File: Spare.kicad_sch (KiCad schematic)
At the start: 9 parts, among them U14 74LS125, U2 74LS14, U26 74LS06, U34 74LS393, U39 74LS04, U49 74LS07N, U5 74LS02, U59 74LS32, U8 74LS08

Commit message: rev 1.0
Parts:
- removed U34: 74LS393, Custom:STD_DDW_DIP14, symbol 74xx:74LS393
- removed U49: 74LS07N, Custom:STD_DDW_DIP14, symbol 74xx:74LS07
- removed U59: 74LS32, Custom:STD_DDW_DIP14, symbol 74xx:74LS32
- added unit 2 of U8
- added unit 1 of U8
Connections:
- no-connect marks 44 -> 34
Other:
- moved on the sheet: U39E

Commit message: V1
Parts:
- removed U39: 74LS04, Custom:STD_DDW_DIP14, symbol 74xx:74LS04
- removed unit 2 of U5
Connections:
- no-connect marks 34 -> 29
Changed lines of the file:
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@@
-	)
-	(no_connect
-		(at 231.14 124.46)
-	)
-	(no_connect
-		(at 299.72 101.6)
 	)
 	(no_connect
@@
 	)
 	(no_connect
-		(at 231.14 129.54)
-	)
-	(no_connect
 		(at 246.38 93.98)
 	)
@@
 	)
 	(no_connect
-		(at 246.38 127)
-	)
-	(no_connect
 		(at 246.38 83.82)
 	)
@@
 	)
 	(no_connect
-		(at 314.96 101.6)
-	)
-	(no_connect
 		(at 278.13 105.41)
 	)
@@
 	(no_connect
 		(at 318.77 101.6)
-	)
-	(symbol
-		(lib_id "74xx:74LS04")
-		(at 307.34 101.6 0)
-		(unit 5)
-		(exclude_from_sim no)
-		(in_bom yes)
-		(on_board yes)
-		(dnp no)
-		(property "Reference" "U39"
-			(at 307.086 99.822 0)
-			(effects
-				(font
-					(size 1.524 1.524)
-				)
-			)
-		)
-		(property "Value" "74LS04"
-			(at 307.594 103.632 0)
-			(effects
-				(font
-					(size 1.524 1.524)
-				)
-			)
-		)
-		(property "Footprint" "Custom:STD_DDW_DIP14"
-			(at 307.34 101.6 0)
-			(effects
-				(font
-					(size 1.27 1.27)
-				)
-				(hide yes)
-			)
-		)
-		(property "Datasheet" "http://www.ti.com/lit/gpn/sn74LS04"
-			(at 307.34 101.6 0)
-			(effects
-				(font
-					(size 1.27 1.27)
-				)
-				(hide yes)
-			)
-		)
-		(property "Description" "Hex Inverter"
-			(at 307.34 101.6 0)
-			(effects
-				(font
-					(size 1.27 1.27)
-				)
-				(hide yes)
-			)
-		)
-		(pin "14"
-		)
-		(pin "7"
-		)
-		(pin "1"
-		)
-		(pin "2"
-		)
-		(pin "3"
-		)
-		(pin "4"
-		)
-		(pin "10"
-		)
-		(pin "9"
-		)
-		(pin "11"
-		)
-		(pin "8"
-		)
-		(pin "12"
-		)
-		(pin "5"
-		)
-		(pin "13"
-		)
-		(pin "6"
-		)
-		(instances
-			(project "N8PC"
-				(path "/d94f9d60-5ece-4752-b49c-b0d1c95f35bc/00000000-0000-0000-0000-0000526d48aa"
-					(reference "U39")
-					(unit 5)
-				)
-			)
-		)
 	)
 	(symbol
@@
 				)
 			)
-		)
-	)
-	(symbol
-		(lib_id "74xx:74LS02")
-		(at 238.76 127 0)
-		(unit 2)
-		(exclude_from_sim no)
-		(in_bom yes)
-		(on_board yes)
-		(dnp no)
-		(property "Reference" "U5"
-			(at 238.76 125.73 0)
-			(effects
-				(font
-					(size 1.524 1.524)
-				)
-			)
-		)
-		(property "Value" "74LS02"
-			(at 238.506 128.27 0)
-			(effects
-				(font
-					(size 1.524 1.524)
-				)
-			)
-		)
-		(property "Footprint" "Custom:STD_DDW_DIP14"
-			(at 238.76 127 0)
-			(effects
-				(font
-					(size 1.27 1.27)
-				)
-				(hide yes)
-			)
-		)
-		(property "Datasheet" "http://www.ti.com/lit/gpn/sn74ls02"
-			(at 238.76 127 0)
-			(effects
-				(font
-					(size 1.27 1.27)
-				)
-				(hide yes)
-			)
-		)
-		(property "Description" "quad 2-input NOR gate"
-			(at 238.76 127 0)
-			(effects
-				(font
-					(size 1.27 1.27)
-				)
-				(hide yes)
-			)
-		)
-		(pin "7"
-		)
-		(pin "2"
-		)
-		(pin "1"
-		)
-		(pin "14"
-		)
-		(pin "3"
-		)
-		(pin "4"
-		)
-		(pin "6"
-		)
-		(pin "10"
-		)
-		(pin "13"
-		)
-		(pin "9"
-		)
-		(pin "5"
-		)
-		(pin "12"
-		)
-		(pin "8"
-		)
-		(pin "11"
-		)
-		(instances
-			(project "N8PC"
-				(path "/d94f9d60-5ece-4752-b49c-b0d1c95f35bc/00000000-0000-0000-0000-0000526d48aa"
-					(reference "U5")
-					(unit 2)
-				)
-			)

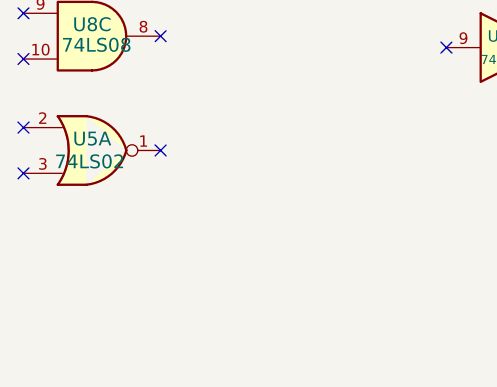
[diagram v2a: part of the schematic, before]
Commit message: V1.1 PCB and schematic fix issue with data direction for bus
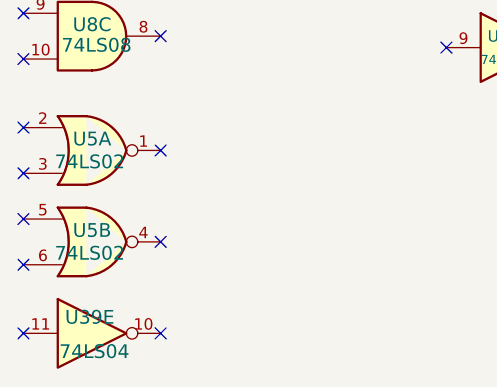
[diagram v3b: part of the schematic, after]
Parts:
- added U39: 74LS04, Custom:STD_DDW_DIP14, symbol 74xx:74LS04
- added unit 2 of U5
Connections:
- no-connect marks 29 -> 34
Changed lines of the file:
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@@
 	(title_block
 		(title "N8PC")
-		(date "2025-11-26")
-		(rev "000.9")
+		(date "2025-12-13")
+		(rev "001.1")
 		(comment 1 "https://github.com/danwerner21/N8PC")
 		(comment 2 "Based on work by Andrew Lynch and John Coffman")
@@
 	)
 	(no_connect
+		(at 231.14 124.46)
+	)
+	(no_connect
 		(at 314.96 81.28)
 	)
@@
 	)
 	(no_connect
+		(at 246.38 137.16)
+	)
+	(no_connect
 		(at 278.13 82.55)
 	)
@@
 	)
 	(no_connect
+		(at 231.14 137.16)
+	)
+	(no_connect
 		(at 299.72 81.28)
 	)
 	(no_connect
+		(at 246.38 127)
+	)
+	(no_connect
 		(at 246.38 116.84)
 	)
@@
 	)
 	(no_connect
+		(at 231.14 129.54)
+	)
+	(no_connect
 		(at 231.14 81.28)
 	)
@@
 	(no_connect
 		(at 318.77 101.6)
+	)
+	(symbol
+		(lib_id "74xx:74LS02")
+		(at 238.76 127 0)
+		(unit 2)
+		(exclude_from_sim no)
+		(in_bom yes)
+		(on_board yes)
+		(dnp no)
+		(property "Reference" "U5"
+			(at 238.76 125.73 0)
+			(effects
+				(font
+					(size 1.524 1.524)
+				)
+			)
+		)
+		(property "Value" "74LS02"
+			(at 238.506 128.27 0)
+			(effects
+				(font
+					(size 1.524 1.524)
+				)
+			)
+		)
+		(property "Footprint" "Custom:STD_DDW_DIP14"
+			(at 238.76 127 0)
+			(effects
+				(font
+					(size 1.27 1.27)
+				)
+				(hide yes)
+			)
+		)
+		(property "Datasheet" "http://www.ti.com/lit/gpn/sn74ls02"
+			(at 238.76 127 0)
+			(effects
+				(font
+					(size 1.27 1.27)
+				)
+				(hide yes)
+			)
+		)
+		(property "Description" "quad 2-input NOR gate"
+			(at 238.76 127 0)
+			(effects
+				(font
+					(size 1.27 1.27)
+				)
+				(hide yes)
+			)
+		)
+		(pin "7"
+		)
+		(pin "2"
+		)
+		(pin "1"
+		)
+		(pin "14"
+		)
+		(pin "3"
+		)
+		(pin "4"
+		)
+		(pin "6"
+		)
+		(pin "10"
+		)
+		(pin "13"
+		)
+		(pin "9"
+		)
+		(pin "5"
+		)
+		(pin "12"
+		)
+		(pin "8"
+		)
+		(pin "11"
+		)
+		(instances
+			(project "N8PC"
+				(path "/d94f9d60-5ece-4752-b49c-b0d1c95f35bc/00000000-0000-0000-0000-0000526d48aa"
+					(reference "U5")
+					(unit 2)
+				)
+			)
+		)
 	)
 	(symbol
@@
 				)
 			)
+		)
+	)
+	(symbol
+		(lib_id "74xx:74LS04")
+		(at 238.76 137.16 0)
+		(unit 5)
+		(exclude_from_sim no)
+		(in_bom yes)
+		(on_board yes)
+		(dnp no)
+		(property "Reference" "U39"
+			(at 238.506 135.382 0)
+			(effects
+				(font
+					(size 1.524 1.524)
+				)
+			)
+		)
+		(property "Value" "74LS04"
+			(at 239.014 139.192 0)
+			(effects
+				(font
+					(size 1.524 1.524)
+				)
+			)
+		)
+		(property "Footprint" "Custom:STD_DDW_DIP14"
+			(at 238.76 137.16 0)
+			(effects
+				(font
+					(size 1.27 1.27)
+				)
+				(hide yes)
+			)
+		)
+		(property "Datasheet" "http://www.ti.com/lit/gpn/sn74LS04"
+			(at 238.76 137.16 0)
+			(effects
+				(font
+					(size 1.27 1.27)
+				)
+				(hide yes)
+			)
+		)
+		(property "Description" "Hex Inverter"
+			(at 238.76 137.16 0)
+			(effects
+				(font
+					(size 1.27 1.27)
+				)
+				(hide yes)
+			)
+		)
+		(pin "14"
+		)
+		(pin "7"
+		)
+		(pin "1"
+		)
+		(pin "2"
+		)
+		(pin "3"
+		)
+		(pin "4"
+		)
+		(pin "10"
+		)
+		(pin "9"
+		)
+		(pin "11"
+		)
+		(pin "8"
+		)
+		(pin "12"
+		)
+		(pin "5"
+		)
+		(pin "13"
+		)
+		(pin "6"
+		)
+		(instances
+			(project "N8PC"
+				(path "/d94f9d60-5ece-4752-b49c-b0d1c95f35bc/00000000-0000-0000-0000-0000526d48aa"
+					(reference "U39")
+					(unit 5)
+				)
+			)
